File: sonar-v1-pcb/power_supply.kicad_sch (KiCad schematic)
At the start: 1 part, among them U52 STUSB4500QTR

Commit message: fix bandpass
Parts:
- removed U52: STUSB4500QTR, symbol sonar_lib:STUSB4500QTR
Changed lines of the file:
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@@
-		)
-	)
-	(symbol
-		(lib_id "sonar_lib:STUSB4500QTR")
-		(at 143.51 111.76 0)
-		(unit 1)
-		(exclude_from_sim no)
-		(in_bom yes)
-		(on_board yes)
-		(dnp no)
-		(fields_autoplaced yes)
-		(property "Reference" "U52"
-			(at 143.51 87.63 0)
-			(effects
-				(font
-					(size 1.524 1.524)
-				)
-			)
-		)
-		(property "Value" "STUSB4500QTR"
-			(at 143.51 90.17 0)
-			(effects
-				(font
-					(size 1.524 1.524)
-				)
-			)
-		)
-		(property "Footprint" ""
-			(at 143.764 135.636 0)
-			(effects
-				(font
-					(size 1.27 1.27)
-					(italic yes)
-				)
-				(hide yes)
-			)
-		)
-		(property "Datasheet" "https://www.st.com/resource/en/datasheet/stusb4500.pdf"
-			(at 143.256 132.842 0)
-			(effects
-				(font
-					(size 1.27 1.27)
-					(italic yes)
-				)
-				(hide yes)
-			)
-		)
-		(property "Description" ""
-			(at 143.51 111.76 0)
-			(effects
-				(font
-					(size 1.27 1.27)
-				)
-				(hide yes)
-			)
-		)
-		(pin "9"
-		)
-		(pin "8"
-		)
-		(pin "17"
-		)
-		(pin "19"
-		)
-		(pin "11"
-		)
-		(pin "15"
-		)
-		(pin "20"
-		)
-		(pin "14"
-		)
-		(pin "2"
-		)
-		(pin "1"
-		)
-		(pin "4"
-		)
-		(pin "5"
-		)
-		(pin "3"
-		)
-		(pin "24"
-		)
-		(pin "21"
-		)
-		(pin "23"
-		)
-		(pin "22"
-		)
-		(pin "25"
-		)
-		(pin "10"
-		)
-		(pin "18"
-		)
-		(pin "16"
-		)
-		(pin "7"
-		)
-		(pin "6"
-		)
-		(pin "13"
-		)
-		(pin "12"
-		)
-		(instances
-			(project ""
-				(path "/f72ceae0-eee4-4385-b0e8-639846bcb5f2/0971c334-b681-41ae-ad35-a89520df0687"
-					(reference "U52")
-					(unit 1)
-				)
-			)
 		)
 	)

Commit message: kept cooking
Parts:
- added C97: 4.7nF, symbol Device:C
- added F1: 1.1A, Diode_SMD:D_1206_3216Metric, symbol Device:Fuse
- added J1: USB_C_Receptacle_PowerOnly_6P, symbol Connector:USB_C_Receptacle_PowerOnly_6P
- added R133, R134: 5.1k, symbol Device:R_US
- added SW1: SW_SPDT, symbol Switch:SW_SPDT
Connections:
- new net: J1.B5 (CC2), R133.1
- new net: C97.1, J1.S1 (SHIELD)
- new net: J1.A5 (CC1), R134.1
- new net: F1.1, J1.A9 (VBUS), J1.B9 (VBUS)
- new net 5v_12v_boost/enable: SW1.2 (B)
- new net GND: C97.2, J1.A12 (GND), J1.B12 (GND), R133.2, R134.2, SW1.1 (A)
- new net VBUS: F1.2, SW1.3 (C)
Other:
- added sheet 5v_12v_boost (5_to_10_boost.kicad_sch)
- note added: "2.2A trip"
- note added: "??? inverting buck boost"
- note added: "Holy fucking yikes is this gonna be a mess"
- note added: "TPS629210 to buck down to 4V"
- note added: "TPS629210 to buck down to 5.5V"
- note added: "TPS7A20 looks sick as fuck for an LDO"
- note added: "TPS7A30 NEGTAIVE LDO for -2.5V"

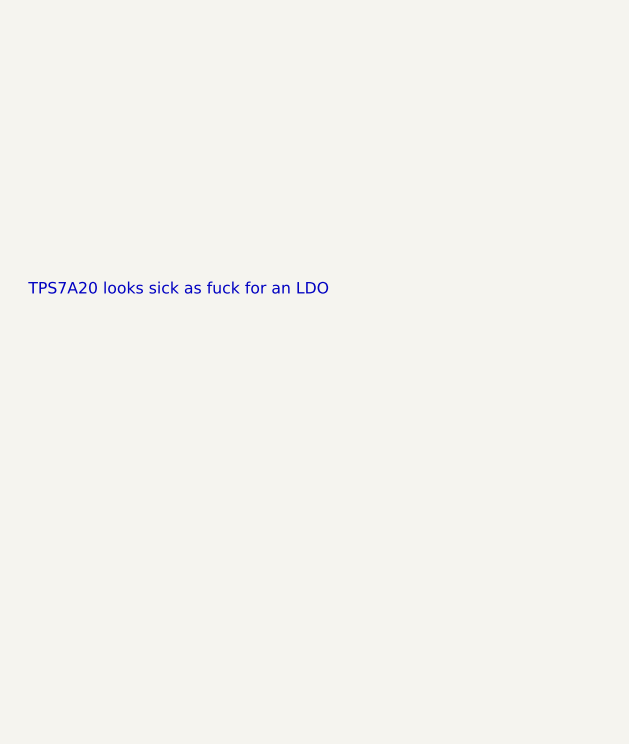
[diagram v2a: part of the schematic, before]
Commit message: Switch to audio not just ultrasonic.
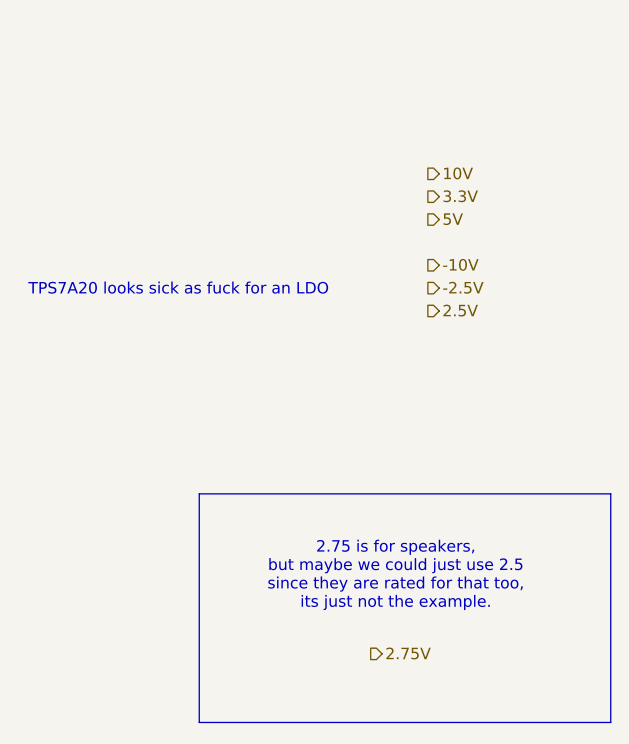
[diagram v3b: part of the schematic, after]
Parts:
- C97: footprint (none) -> Capacitor_SMD:C_0402_1005Metric
- R133, R134: footprint (none) -> Resistor_SMD:R_0402_1005Metric
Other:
- note added: "2.75 is for speakers, but maybe we could just use 2.5 since they are rated for that too, its just not the example."
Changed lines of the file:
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@@
 	(generator_version "9.0")
 	(paper "A4")
+	(rectangle
+		(start 231.14 101.6)
+		(end 276.86 127)
+		(stroke
+			(width 0)
+			(type default)
+		)
+		(fill
+			(type none)
+		)
+	)
 	(text "TPS7A30 NEGTAIVE LDO for -2.5V"
 		(exclude_from_sim no)
@@
 			(font
 				(size 1.27 1.27)
+			)
+		)
+	)
+	(text "2.75 is for speakers, \nbut maybe we could just use 2.5 \nsince they are rated for that too, \nits just not the example."
+		(exclude_from_sim no)
+		(at 252.984 110.744 0)
+		(effects
+			(font
+				(size 1.27 1.27)
+				(color 194 0 0 1)
 			)
 		)
@@
 		)
 	)
+	(hierarchical_label "3.3V"
+		(shape output)
+		(at 256.54 68.58 0)
+		(effects
+			(font
+				(size 1.27 1.27)
+			)
+			(justify left)
+		)
+	)
+	(hierarchical_label "-10V"
+		(shape output)
+		(at 256.54 76.2 0)
+		(effects
+			(font
+				(size 1.27 1.27)
+			)
+			(justify left)
+		)
+	)
+	(hierarchical_label "2.5V"
+		(shape output)
+		(at 256.54 81.28 0)
+		(effects
+			(font
+				(size 1.27 1.27)
+			)
+			(justify left)
+		)
+	)
+	(hierarchical_label "10V"
+		(shape output)
+		(at 256.54 66.04 0)
+		(effects
+			(font
+				(size 1.27 1.27)
+			)
+			(justify left)
+		)
+	)
+	(hierarchical_label "2.75V"
+		(shape output)
+		(at 250.19 119.38 0)
+		(effects
+			(font
+				(size 1.27 1.27)
+			)
+			(justify left)
+		)
+	)
+	(hierarchical_label "-2.5V"
+		(shape output)
+		(at 256.54 78.74 0)
+		(effects
+			(font
+				(size 1.27 1.27)
+			)
+			(justify left)
+		)
+	)
 	(hierarchical_label "GND"
 		(shape output)
@@
 		(shape output)
 		(at 90.17 66.04 90)
+		(effects
+			(font
+				(size 1.27 1.27)
+			)
+			(justify left)
+		)
+	)
+	(hierarchical_label "5V"
+		(shape output)
+		(at 256.54 71.12 0)
 		(effects
 			(font
@@
 			)
 		)
-		(property "Footprint" ""
+		(property "Footprint" "Resistor_SMD:R_0402_1005Metric"
 			(at 74.676 94.234 90)
 			(effects
@@
 			)
 		)
-		(property "Footprint" ""
+		(property "Footprint" "Capacitor_SMD:C_0402_1005Metric"
 			(at 49.2252 107.95 0)
 			(effects
@@
 			)
 		)
-		(property "Footprint" ""
+		(property "Footprint" "Resistor_SMD:R_0402_1005Metric"
 			(at 86.106 94.234 90)
 			(effects

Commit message: Josh cooking some more.
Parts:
- added C2901, C2902, C2914, C2915: 1uF, Capacitor_SMD:C_0402_1005Metric, symbol Device:C
- added C2903, C2904: 1uF, symbol Device:C
- added C2905, C2906, C2907, C2908, C2909: 22uF, Capacitor_SMD:C_0402_1005Metric, symbol Device:C
- added C2910: 470nF, Capacitor_SMD:C_0402_1005Metric, symbol Device:C
- added C2911: 2.2nF, Capacitor_SMD:C_0402_1005Metric, symbol Device:C
- added C2912, C2913: 10uF, Capacitor_SMD:C_0402_1005Metric, symbol Device:C
- added C2917: 0.1uF, Capacitor_SMD:C_0402_1005Metric, symbol Device:C
- added FB2901: FerriteBead, symbol Device:FerriteBead
- added L2901: 2.2uH, Inductor_SMD:L_0402_1005Metric, symbol Device:L
- added TP2901, TP2902, TP2903, TP2904, TP2905, TP2906, TP2907: TestPoint_Probe, TestPoint:TestPoint_Pad_D1.0mm, symbol Connector:TestPoint_Probe
- added U2901: TPS7A2033DQN, Package_SON:Texas_X2SON-4_1x1mm_P0.65mm, symbol Regulator_Linear:TPS7A20xxxDQN
- added U2902: TPS7A2028DQN, Package_SON:Texas_X2SON-4_1x1mm_P0.65mm, symbol Regulator_Linear:TPS7A20xxxDQN
- added U2903: TPS62912, Package_DFN_QFN:Texas_RPU0010A_VQFN-HR-10_2x2mm_P0.5mm, symbol Regulator_Switching:TPS62912
- added U2904: TPS7A205DQN, Package_SON:Texas_X2SON-4_1x1mm_P0.65mm, symbol Regulator_Linear:TPS7A20xxxDQN
- added U2905: TPS7A91, Package_DFN_QFN:Texas_S-PDSO-N10_EP1.2x2mm, symbol Regulator_Linear:TPS7A91
- J2901: renamed from J1; footprint (none) -> Connector_TE-Connectivity:TE_2834006-1_1x01_P4.0mm_Horizontal
- renumbered C97 to C2916, F1 to F2901, R133 to R2901, R134 to R2902, SW1 to SW2901
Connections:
- net 3.3V: now also C2901.1, C2904.2, TP2901.1, U2901.1 (OUT), U2902.3 (EN), U2902.4 (IN)
- net 5V: now also C2914.1, TP2905.1, U2904.1 (OUT)
- net 5v_12v_boost/12V: now also C2910.1, C2911.1, C2912.1, C2913.1, U2903.1 (EN/SYNC), U2903.10 (S-CONF), U2903.6 (VIN)
- net GND: now also C2901.2, C2902.1, C2903.2, C2904.1, C2905.1, C2906.1, C2907.1, C2908.1, C2909.1, C2911.2, C2912.2, C2913.2, C2914.2, C2915.1, C2917.1, TP2906.1, U2901.2 (GND), U2901.5 (Pad), U2902.2 (GND), U2902.5 (Pad), U2903.4 (PGND), U2903.5 (PG), U2903.7 (PSNS), U2904.2 (GND), U2904.5 (Pad), U2905.11 (GND), U2905.4 (GND)
- net VBUS: now also TP2904.1
- net at F2901.1, J2901.A9 (VBUS), J2901.B9 (VBUS): now also TP2903.1
- new net: C2917.2, U2905.8 (NR/SS)
- new net: L2901.1, U2903.2 (SW)
- new net: C2905.2, C2906.2, C2907.2, FB2901.1, L2901.2
- new net: C2910.2, U2903.8 (NR/SS)
- new net: U2905.1 (OUT), U2905.2 (OUT)
- new net 2.8V: C2903.1, TP2902.1, U2902.1 (OUT)
- new net 5.5V: C2902.2, C2908.2, C2909.2, C2915.2, FB2901.2, U2901.3 (EN), U2901.4 (IN), U2904.3 (EN), U2904.4 (IN), U2905.10 (IN), U2905.7 (EN), U2905.9 (IN)
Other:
- note added: "600mA required for 2.5V bus, so use a TPS7A91 instead"
- note added: "Holy lost in the sauce... I am gonna let you fix this one George"
- note added: "Max 1.5mA from audio RX"
- note added: "Max 150mA from ADC AVDD"
- note added: "TODO: design the feedback loop"
- note added: "look at https://www.ti.com/lit/an/sbva042/sbva042.pdf?ts=1773012729035 before connecting to the LDOs"
- note removed: "2.75 is for speakers, but maybe we could just use 2.5 since they are rated for that too, its just not the example."

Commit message: Start on power circuitry
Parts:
- removed C2916: 4.7nF, Capacitor_SMD:C_0402_1005Metric, symbol Device:C
- removed F2901: 1.1A, Diode_SMD:D_1206_3216Metric, symbol Device:Fuse
- removed J2901: USB_C_Receptacle_PowerOnly_6P, Connector_TE-Connectivity:TE_2834006-1_1x01_P4.0mm_Horizontal, symbol Connector:USB_C_Receptacle_PowerOnly_6P
- removed R2901, R2902: 5.1k, Resistor_SMD:R_0402_1005Metric, symbol Device:R_US
- removed TP2903, TP2904, TP2906: TestPoint_Probe, TestPoint:TestPoint_Pad_D1.0mm, symbol Connector:TestPoint_Probe
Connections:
- net GND: no longer SW2901.1 (A)
- net VBUS renamed Vin
- new net 5v_12v_boost/GND: SW2901.1 (A)
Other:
- note removed: "2.2A trip"
- moved on the sheet: C2901, C2902, C2903, C2904, C2905, C2906, C2907, C2908, C2909, C2910, C2911, C2912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

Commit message: Do some more power work and add a few components
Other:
- added sheet 12V_to_10V_LDO (12v_to_10v_ldo.kicad_sch)
- added sheet 5V_to_-12V_inverting_buck_boost (inverting_buck_boost.kicad_sch)
- added sheet 5V_to_12V_boost (5v_to_12v_boost.kicad_sch)
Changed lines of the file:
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@@
 		)
 	)
+	(text_box "Not actually 12V but figure out the dropout voltage on the LDO"
+		(exclude_from_sim no)
+		(at 182.88 43.18 0)
+		(size 30.48 10.16)
+		(margins 0.9525 0.9525 0.9525 0.9525)
+		(stroke
+			(width 0)
+			(type solid)
+		)
+		(fill
+			(type none)
+		)
+		(effects
+			(font
+				(size 1.27 1.27)
+			)
+			(justify left top)
+		)
+	)
 	(junction
 		(at 716.28 68.58)
@@
 	(hierarchical_label "Vin"
 		(shape input)
-		(at 128.27 92.71 180)
+		(at 111.76 88.9 180)
 		(effects
 			(font
@@
 	)
 	(sheet
+		(at 139.7 83.82)
+		(size 27.94 7.62)
+		(exclude_from_sim no)
+		(in_bom yes)
+		(on_board yes)
+		(dnp no)
+		(fields_autoplaced yes)
+		(stroke
+			(width 0.1524)
+			(type solid)
+		)
+		(fill
+			(color 255 128 143 1.0000)
+		)
+		(property "Sheetname" "5V_to_12V_boost"
+			(at 139.7 83.1084 0)
+			(effects
+				(font
+					(size 1.27 1.27)
+				)
+				(justify left bottom)
+			)
+		)
+		(property "Sheetfile" "5v_to_12v_boost.kicad_sch"
+			(at 139.7 92.0246 0)
+			(effects
+				(font
+					(size 1.27 1.27)
+				)
+				(justify left top)
+			)
+		)
+		(instances
+			(project "sonar"
+				(path "/f72ceae0-eee4-4385-b0e8-639846bcb5f2/0971c334-b681-41ae-ad35-a89520df0687"
+					(page "33")
+				)
+			)
+		)
+	)
+	(sheet
 		(at 502.92 91.44)
 		(size 27.94 26.67)
@@
 				)
 			)
+		)
+	)
+	(sheet
+		(at 139.7 110.49)
+		(size 27.94 8.89)
+		(exclude_from_sim no)
+		(in_bom yes)
+		(on_board yes)
+		(dnp no)
+		(fields_autoplaced yes)
+		(stroke
+			(width 0.1524)
+			(type solid)
+		)
+		(fill
+			(color 255 128 143 1.0000)
+		)
+		(property "Sheetname" "5V_to_-12V_inverting_buck_boost"
+			(at 139.7 109.7784 0)
+			(effects
+				(font
+					(size 1.27 1.27)
+				)
+				(justify left bottom)
+			)
+		)
+		(property "Sheetfile" "inverting_buck_boost.kicad_sch"
+			(at 139.7 119.9646 0)
+			(effects
+				(font
+					(size 1.27 1.27)
+				)
+				(justify left top)
+			)
+		)
+		(instances
+			(project "sonar"
+				(path "/f72ceae0-eee4-4385-b0e8-639846bcb5f2/0971c334-b681-41ae-ad35-a89520df0687"
+					(page "35")
+				)
+			)
+		)
+	)
+	(sheet
+		(at 186.69 58.42)
+		(size 25.4 22.86)
+		(exclude_from_sim no)
+		(in_bom yes)
+		(on_board yes)
+		(dnp no)
+		(fields_autoplaced yes)
+		(stroke
+			(width 0.1524)
+			(type solid)
+		)
+		(fill
+			(color 255 128 143 1.0000)
+		)
+		(property "Sheetname" "12V_to_10V_LDO"
+			(at 186.69 57.7084 0)
+			(effects
+				(font
+					(size 1.27 1.27)
+				)
+				(justify left bottom)
+			)
+		)
+		(property "Sheetfile" "12v_to_10v_ldo.kicad_sch"
+			(at 186.69 81.8646 0)
+			(effects
+				(font
+					(size 1.27 1.27)
+				)
+				(justify left top)
+			)
+		)
+		(instances
+			(project "sonar"
+				(path "/f72ceae0-eee4-4385-b0e8-639846bcb5f2/0971c334-b681-41ae-ad35-a89520df0687"
+					(page "34")
+				)
+			)

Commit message: wip
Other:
- sheet 5V_to_-12V_inverting_buck_boost renamed Vin to -12V Inverting Buck Boost
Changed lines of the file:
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@@
 	)
 	(sheet
-		(at 139.7 110.49)
-		(size 27.94 8.89)
+		(at 135.89 111.76)
+		(size 34.29 24.13)
 		(exclude_from_sim no)
 		(in_bom yes)
@@
 			(color 255 128 143 1.0000)
 		)
-		(property "Sheetname" "5V_to_-12V_inverting_buck_boost"
-			(at 139.7 109.7784 0)
+		(property "Sheetname" "Vin to -12V Inverting Buck Boost"
+			(at 135.89 111.0484 0)
 			(effects
 				(font
@@
 		)
 		(property "Sheetfile" "inverting_buck_boost.kicad_sch"
-			(at 139.7 119.9646 0)
+			(at 135.89 136.4746 0)
 			(effects
 				(font

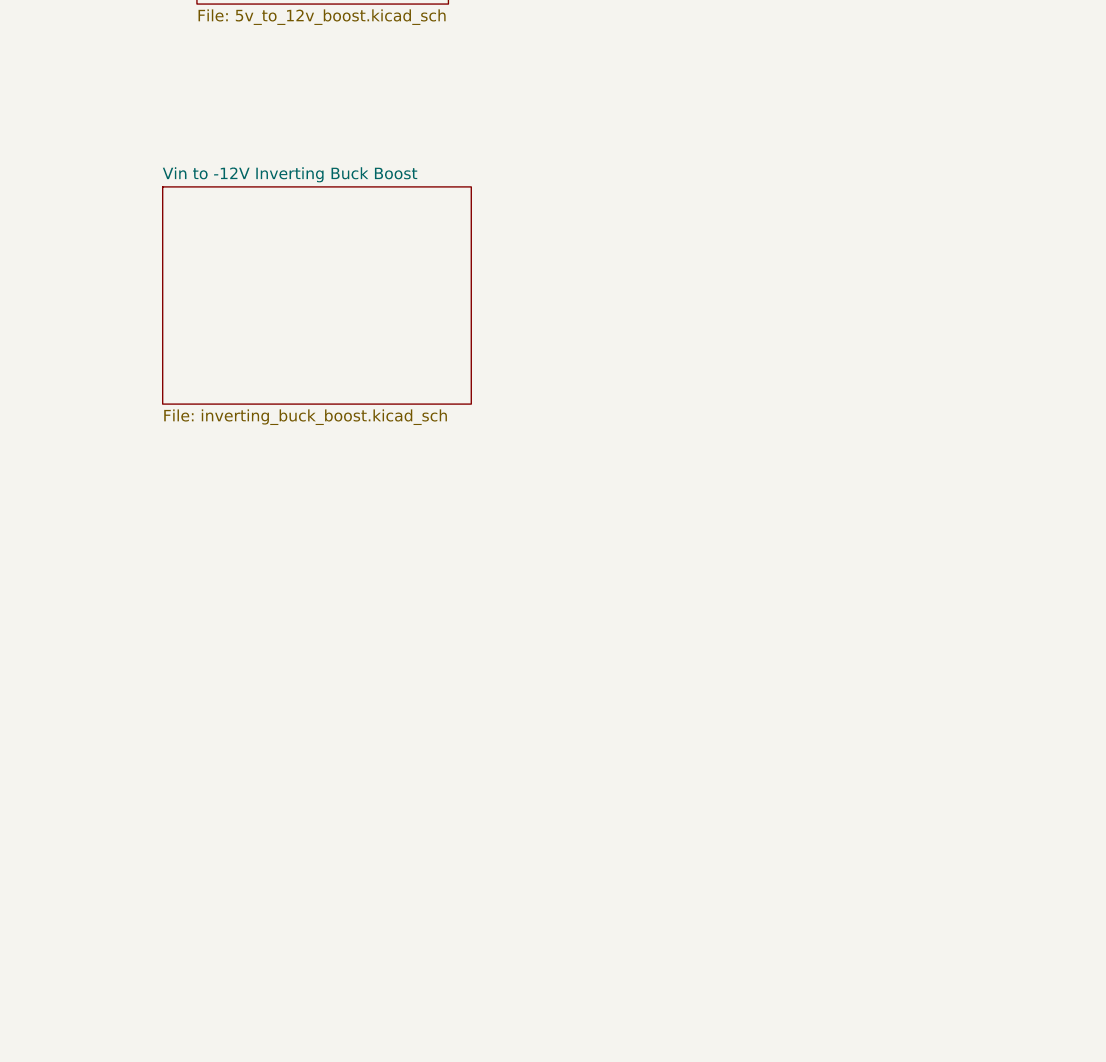
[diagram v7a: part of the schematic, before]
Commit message: Finish -12V buck
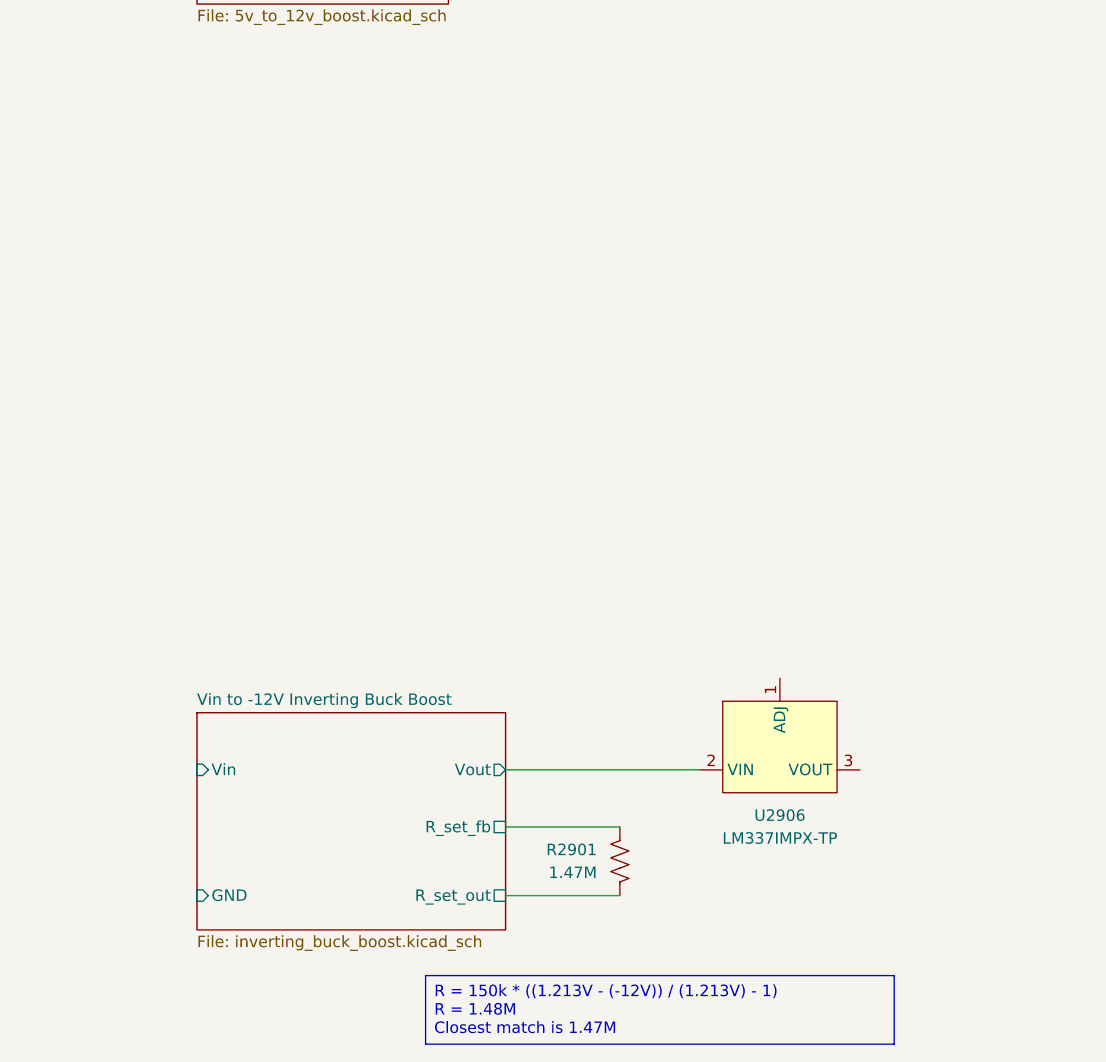
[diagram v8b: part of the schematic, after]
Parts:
- added R2901: 1.47M, Sonar:R_0603_1608Metric, symbol sonar_lib:R_0603_1.47M
- added U2906: LM337IMPX-TP, Sonar:SOT-223, symbol sonar_lib:LM337IMPX-TP
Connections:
- new net Vin to -12V Inverting Buck Boost/R_set_fb: R2901.1
- new net Vin to -12V Inverting Buck Boost/R_set_out: R2901.2
- new net Vin to -12V Inverting Buck Boost/Vout: U2906.2 (VIN), U2906.4 (VIN)
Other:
- sheet Vin to -12V Inverting Buck Boost ports: added GND, R_set_fb, R_set_out, Vin, Vout; removed none
